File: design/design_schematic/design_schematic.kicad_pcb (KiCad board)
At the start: 4 copper layers, 144 x 95.2 mm, 166 parts, among them IC2 XC9148G50CER-G, IC3 nRF52833-QDAA-R7, IC4 74AHCT125PW,118, IC5 MCP23018T-E_SS, IC6 XC9291B33D1R-G, J1 USB_C_Receptacle_USB2.0_16P, J2 Battery Pos, J3 Battery Neg, J4 OLED_128x32, J5 SFV12R-1STBE1HLF, J6 PinHeader_1x04_P2.54mm_Horizo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, U2 BQ24072RGT, U3 USB6B1, U4 BQ27441-G1, U5 PEC11L-4015F-S0015, U6 PEC11L-4015F-S0015, X1 32MHz

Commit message: prepare RS production
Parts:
- added OUT_1: TestPoint, TestPoint:TestPoint_Pad_D1.5mm, F.Cu at (1.27, 1.27)
- renumbered 5V_4 to OUT_1
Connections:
- J6 pad 3: Net-(IC3-SWDCLK) -> Net-(IC3-SWDIO)
- J6 pad 4: Net-(IC3-SWDIO) -> Net-(IC3-SWDCLK)
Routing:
- net Net-(IC3-SWDIO): track 21.8 -> 16.2 mm
- net Net-(IC3-SWDCLK): track 18.7 -> 19.4 mm
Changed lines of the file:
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@@
 			(layers "*.Cu" "*.Mask")
 			(remove_unused_layers no)
-			(net 99 "Net-(IC3-SWDCLK)")
+			(net 90 "Net-(IC3-SWDIO)")
 		)
 		(pad "4" thru_hole oval
@@
 			(layers "*.Cu" "*.Mask")
 			(remove_unused_layers no)
-			(net 90 "Net-(IC3-SWDIO)")
+			(net 99 "Net-(IC3-SWDCLK)")
 		)
 		(model "${KICAD8_3DMODEL_DIR}/Connector_PinHeader_2.54mm.3dshapes/PinHeader_1x04_P2.54mm_Horizontal.wrl"
@@
 		)
 	)
+	(footprint "TestPoint:TestPoint_Pad_D1.5mm"
+		(layer "F.Cu")
+		(at 1.275 1.275)
+		(descr "SMD pad as test Point, diameter 1.5mm")
+		(tags "test point SMD pad")
+		(property "Reference" "OUT_1"
+			(at 0 -1.648 0)
+			(layer "F.SilkS")
+			(effects
+				(font
+					(size 1 1)
+					(thickness 0.15)
+				)
+			)
+		)
+		(property "Value" "TestPoint"
+			(at 0 1.75 0)
+			(layer "F.Fab")
+			(effects
+				(font
+					(size 1 1)
+					(thickness 0.15)
+				)
+			)
+		)
+		(property "Footprint" "TestPoint:TestPoint_Pad_D1.5mm"
+			(at 0 0 0)
+			(unlocked yes)
+			(layer "F.Fab")
+			(hide yes)
+			(effects
+				(font
+					(size 1.27 1.27)
+					(thickness 0.15)
+				)
+			)
+		)
+		(property "Datasheet" ""
+			(at 0 0 0)
+			(unlocked yes)
+			(layer "F.Fab")
+			(hide yes)
+			(effects
+				(font
+					(size 1.27 1.27)
+					(thickness 0.15)
+				)
+			)
+		)
+		(property "Description" "test point"
+			(at 0 0 0)
+			(unlocked yes)
+			(layer "F.Fab")
+			(hide yes)
+			(effects
+				(font
+					(size 1.27 1.27)
+					(thickness 0.15)
+				)
+			)
+		)
+		(property ki_fp_filters "Pin* Test*")
+		(sheetname "Root")
+		(sheetfile "design_schematic.kicad_sch")
+		(attr exclude_from_pos_files)
+		(fp_circle
+			(center 0 0)
+			(end 0 0.95)
+			(stroke
+				(width 0.12)
+				(type solid)
+			)
+			(fill none)
+			(layer "F.SilkS")
+		)
+		(fp_circle
+			(center 0 0)
+			(end 1.25 0)
+			(stroke
+				(width 0.05)
+				(type solid)
+			)
+			(fill none)
+			(layer "F.CrtYd")
+		)
+		(fp_text user "${REFERENCE}"
+			(at 0 -1.65 0)
+			(layer "F.Fab")
+			(effects
+				(font
+					(size 1 1)
+					(thickness 0.15)
+				)
+			)
+		)
+		(pad "1" smd circle
+			(at 0 0)
+			(size 1.5 1.5)
+			(layers "F.Cu" "F.Mask")
+			(net 159 "/OUT")
+			(pinfunction "1")
+			(pintype "passive")
+		)
+	)
 	(footprint "MountingHole:MountingHole_3.2mm_M3"
 		(layer "F.Cu")
@@
 		(descr "SMD pad as test Point, diameter 1.5mm")
 		(tags "test point SMD pad")
-		(property "Reference" "5V_4"
+		(property "Reference" "OUT_1"
 			(at 0 -1.648 0)
 			(layer "F.SilkS")
@@
 	)
 	(via
-		(at 91.7095 116.8024)
+		(at 91.7095 116.3734)
 		(size 1)
 		(drill 0.6)
@@
 	)
 	(segment
-		(start 91.7095 115.7604)
-		(end 91.7095 116.8024)
-		(width 0.5)
-		(layer "B.Cu")
-		(net 1)
-	)
-	(segment
-		(start 90.5925 114.6434)
-		(end 91.7095 115.7604)
-		(width 0.5)
-		(layer "B.Cu")
-		(net 1)
-	)
-	(segment
 		(start 168.759 96.5219)
 		(end 168.7985 96.4824)
@@
 	)
 	(segment
-		(start 91.7095 116.8204)
-		(end 91.7095 116.8024)
-		(width 0.35)
-		(layer "B.Cu")
-		(net 1)
-	)
-	(segment
 		(start 125.8965 40.4734)
 		(end 125.8965 39.3564)
@@
 	)
 	(segment
-		(start 88.4965 120.0234)
-		(end 88.5065 120.0234)
-		(width 0.35)
-		(layer "B.Cu")
-		(net 1)
-	)
-	(segment
 		(start 75.0665 33.5984)
 		(end 75.2215 33.5984)
@@
 	)
 	(segment
+		(start 91.7095 116.3734)
+		(end 91.7095 116.8204)
+		(width 0.35)
+		(layer "B.Cu")
+		(net 1)
+	)
+	(segment
 		(start 105.2855 107.3914)
 		(end 104.6635 106.7694)
@@
 	)
 	(segment
+		(start 91.7095 116.8204)
+		(end 88.5065 120.0234)
+		(width 0.35)
+		(layer "B.Cu")
+		(net 1)
+	)
+	(segment
 		(start 86.6425 106.8964)
 		(end 87.022128 106.8964)
@@
 	)
 	(segment
+		(start 91.7095 115.7604)
+		(end 90.5925 114.6434)
+		(width 0.5)
+		(layer "B.Cu")
+		(net 1)
+	)
+	(segment
 		(start 107.2035 107.3784)
 		(end 106.2885 107.3784)
@@
 	)
 	(segment
-		(start 88.5065 120.0234)
-		(end 91.7095 116.8204)
-		(width 0.35)
-		(layer "B.Cu")
-		(net 1)
-	)
-	(segment
 		(start 149.709 77.4719)
 		(end 149.7485 77.4324)
@@
 	)
 	(segment
+		(start 91.7095 116.3734)
+		(end 91.7095 115.7604)
+		(width 0.5)
+		(layer "B.Cu")
+		(net 1)
+	)
+	(segment
 		(start 150.359808 100.9274)
 		(end 150.095516 100.663108)
@@
 	)
 	(segment
+		(start 88.5065 120.0234)
+		(end 88.4965 120.0234)
+		(width 0.35)
+		(layer "B.Cu")
+		(net 1)
+	)
+	(segment
 		(start 80.124 79.5629)
 		(end 79.559 79.5629)
@@
 	)
 	(segment
-		(start 79.8565 119.4234)
-		(end 81.7425 121.3094)
-		(width 0.2)
-		(layer "B.Cu")
-		(net 90)
-	)
-	(segment
-		(start 79.8565 116.2734)
-		(end 79.8565 119.4234)
-		(width 0.2)
-		(layer "B.Cu")
-		(net 90)
-	)
-	(segment
-		(start 80.1715 115.9584)
-		(end 79.8565 116.2734)
-		(width 0.2)
-		(layer "B.Cu")
-		(net 90)
-	)
-	(segment
-		(start 91.9265 118.3734)
-		(end 93.5765 120.0234)
+		(start 83.4925 121.3094)
+		(end 89.7505 121.3094)
 		(width 0.2)
 		(layer "B.Cu")
@@
 	)
 	(segment
-		(start 91.060154 118.3734)
-		(end 91.9265 118.3734)
+		(start 89.7505 121.3094)
+		(end 91.0365 120.0234)
 		(width 0.2)
 		(layer "B.Cu")
@@
 	)
 	(segment
-		(start 89.738657 120.755557)
-		(end 89.738657 119.694897)
+		(start 79.8565 117.6734)
+		(end 83.4925 121.3094)
 		(width 0.2)
 		(layer "B.Cu")
@@
 	)
 	(segment
-		(start 89.184814 121.3094)
-		(end 89.738657 120.755557)
+		(start 80.1715 115.9584)
+		(end 79.8565 116.2734)
 		(width 0.2)
 		(layer "B.Cu")
@@
 	)
 	(segment
-		(start 89.738657 119.694897)
-		(end 91.060154 118.3734)
-		(width 0.2)
-		(layer "B.Cu")
-		(net 90)
-	)
-	(segment
-		(start 81.7425 121.3094)
-		(end 89.184814 121.3094)
+		(start 79.8565 116.2734)
+		(end 79.8565 117.6734)
 		(width 0.2)
 		(layer "B.Cu")
@@
 	)
 	(segment
-		(start 79.1565 119.9234)
-		(end 80.9425 121.7094)
+		(start 79.7715 115.3584)
+		(end 79.1565 115.9734)
 		(width 0.2)
 		(layer "B.Cu")
@@
 	)
 	(segment
-		(start 80.9425 121.7094)
-		(end 89.3505 121.7094)
+		(start 79.1565 115.9734)
+		(end 79.1565 117.5734)
 		(width 0.2)
 		(layer "B.Cu")
@@
 	)
 	(segment
-		(start 89.3505 121.7094)
-		(end 91.0365 120.0234)
+		(start 83.2925 121.7094)
+		(end 91.8905 121.7094)
 		(width 0.2)
 		(layer "B.Cu")
@@
 	)
 	(segment
-		(start 79.1565 115.9734)
-		(end 79.1565 119.9234)
+		(start 79.1565 117.5734)
+		(end 83.2925 121.7094)
 		(width 0.2)
 		(layer "B.Cu")
@@
 	)
 	(segment
-		(start 79.7715 114.8224)
-		(end 79.7715 115.3584)
+		(start 91.8905 121.7094)
+		(end 93.293657 120.306243)
 		(width 0.2)
 		(layer "B.Cu")
@@
 	)
 	(segment
-		(start 79.7715 115.3584)
-		(end 79.1565 115.9734)
+		(start 79.7715 114.8224)
+		(end 79.7715 115.3584)
 		(width 0.2)
 		(layer "B.Cu")
@@
 		(min_thickness 0.25)
 		(filled_areas_thickness no)
-		(fill yes
+		(fill
 			(thermal_gap 0.5)
 			(thermal_bridge_width 0.5)
@@
 		(polygon
 			(pts
-				(xy 57.4065 23.2034) (xy 205.9525 23.2034) (xy 205.9525 126.588974) (xy 207.40038 120.8664) (xy 104.6065 122.5734)
+				(xy 57.4065 23.2034) (xy 205.9525 23.2034) (xy 205.9525 117.1734) (xy 205.9065 120.8664) (xy 104.6065 122.5734)
 				(xy 57.9565 122.8734) (xy 57.0565 105.7534)
 			)
@@
 		(min_thickness 0.25)
 		(filled_areas_thickness no)
-		(fill
+		(fill yes
 			(thermal_gap 0.5)
 			(thermal_bridge_width 0.5)
@@
 		(polygon
 			(pts
-				(xy 58.697257 102.400157) (xy 76.858257 102.400157) (xy 94.647519 115.16781) (xy 94.641561 123.588185)
+				(xy 58.697257 84.40827) (xy 63.442866 84.379502) (xy 94.647519 115.16781) (xy 94.641561 123.588185)
 				(xy 58.84815 122.950264) (xy 58.824257 119.383117) (xy 58.697257 119.378111)
 			)

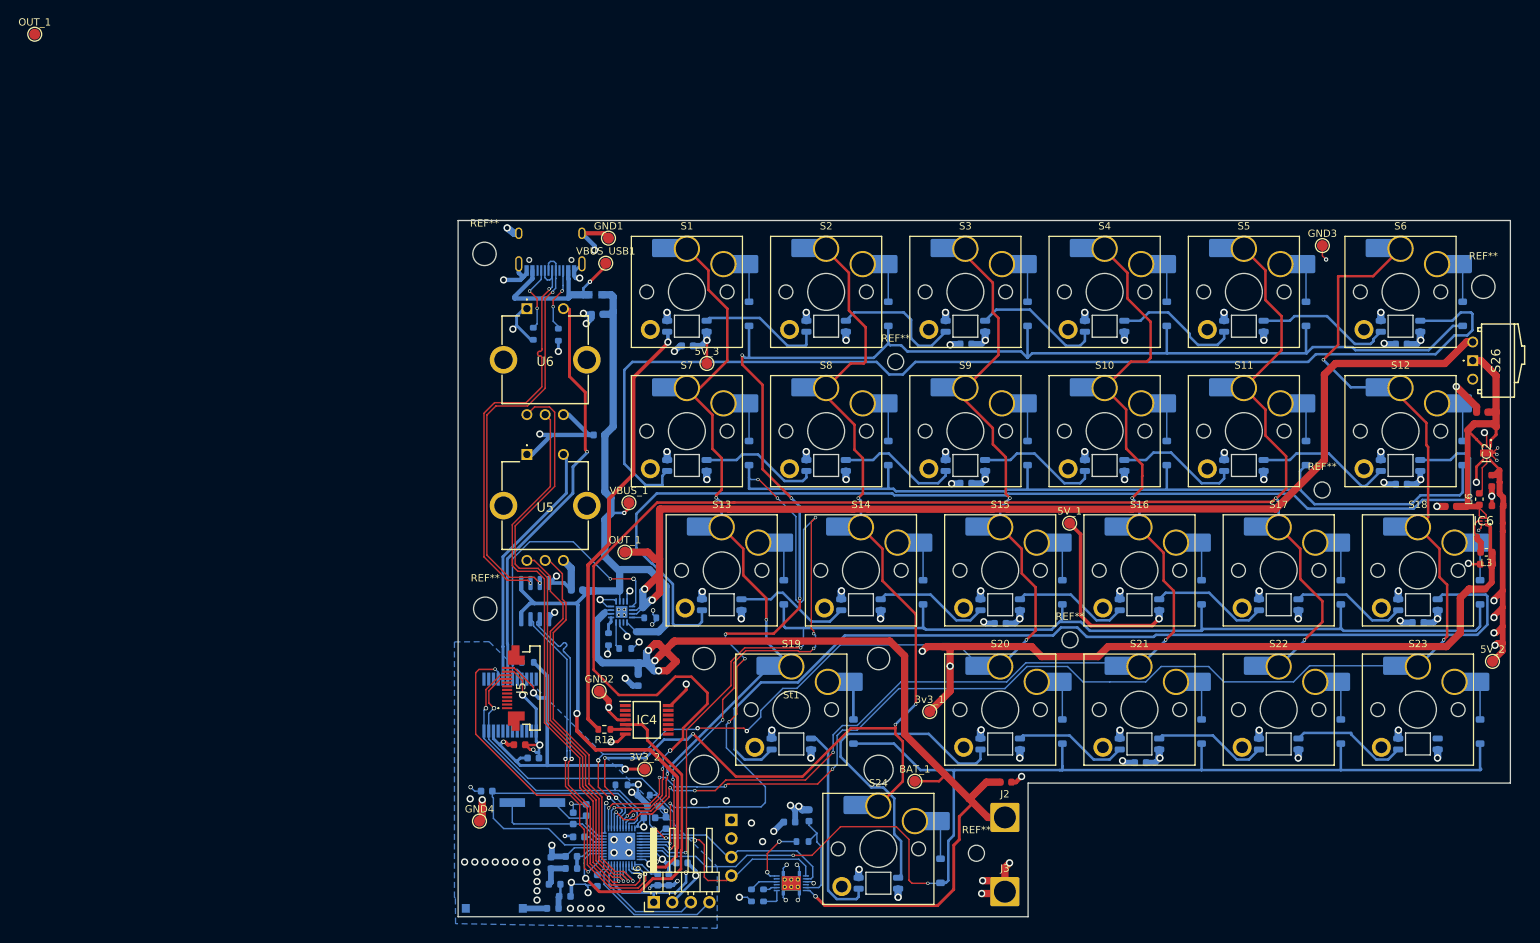
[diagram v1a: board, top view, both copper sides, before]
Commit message: begin to remove unnecessary vias
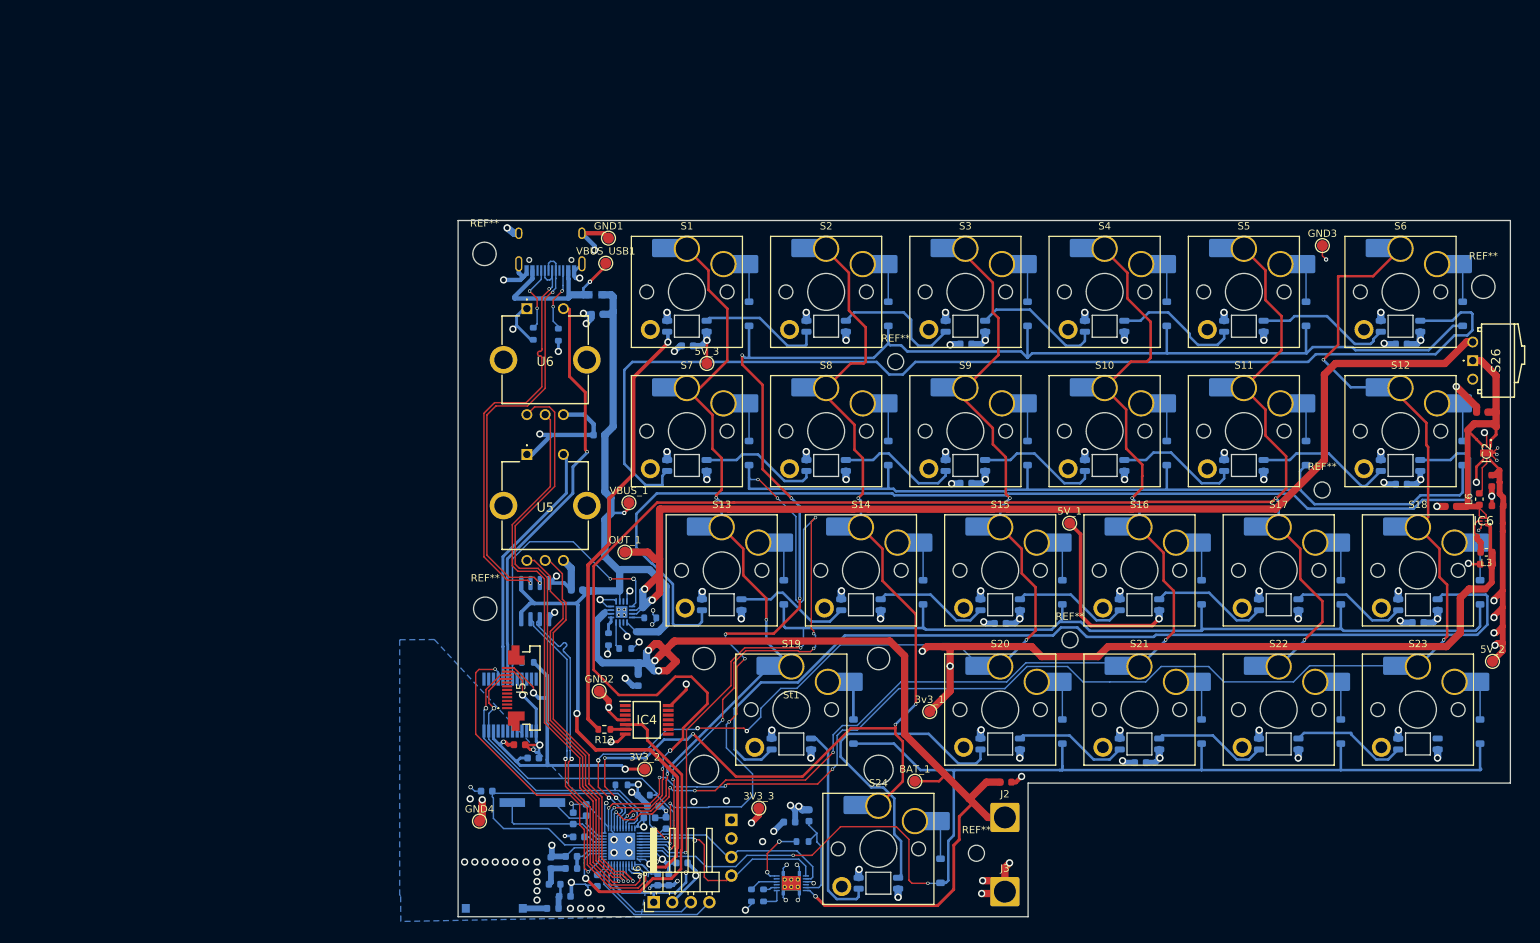
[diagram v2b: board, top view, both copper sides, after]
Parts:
- removed the OUT_1 at (1.27, 1.27)
- added 3V3_3: TestPoint, TestPoint:TestPoint_Pad_D1.5mm, F.Cu at (100.3, 107.1)
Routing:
- net /Row 0: track 221.5 -> 218.5 mm
- net 3V3: track 265.3 -> 267.8 mm
- net GND: track 241.6 -> 242.1 mm

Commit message: production save prepare for left side
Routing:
- net /Column 4: track 226.9 -> 214.6 mm
- net 5V: track 114.5 -> 122.3 mm
- net /Row 0: track 218.5 -> 214.2 mm
- net 3V3: track 267.8 -> 266.5 mm, vias 17 -> 14
- net /Row 1: track 217.4 -> 216.6 mm
- net /Row 2: track 164.4 -> 163.9 mm
- net GND: track 242.1 -> 241.7 mm, vias 116 -> 115
